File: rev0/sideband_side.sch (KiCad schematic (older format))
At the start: 10 parts

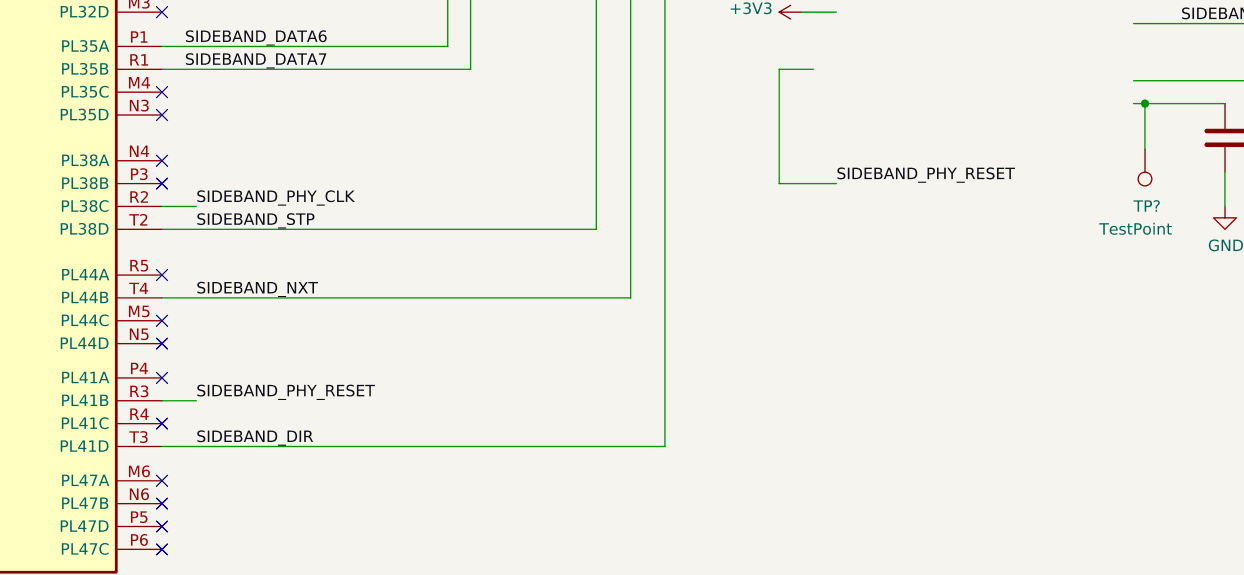
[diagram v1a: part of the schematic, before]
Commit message: schematic: finish initial capture
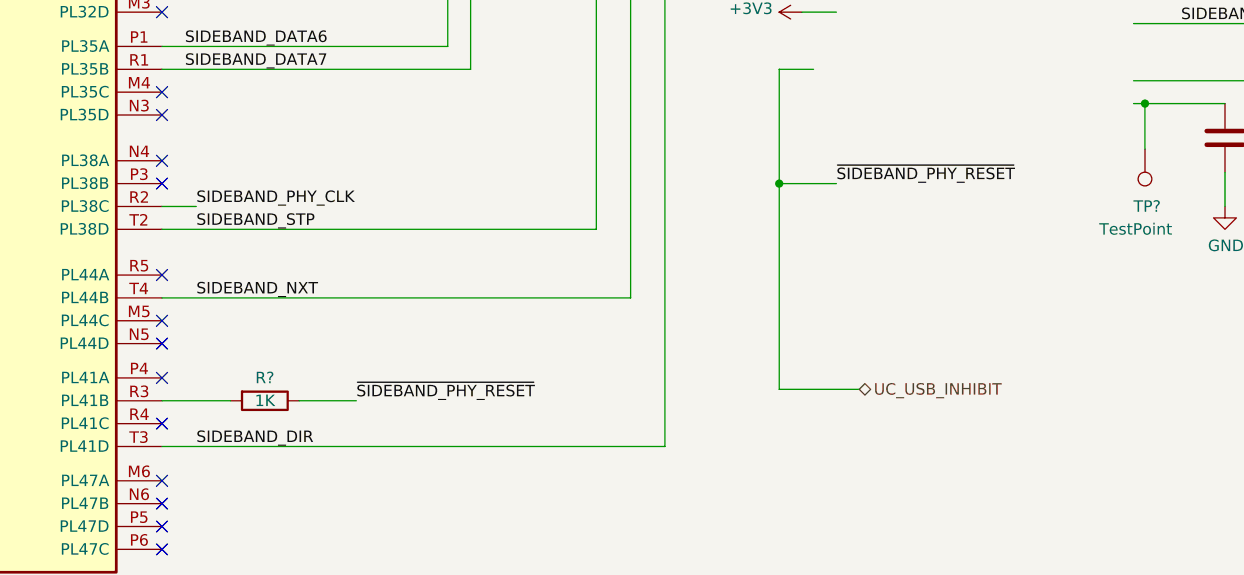
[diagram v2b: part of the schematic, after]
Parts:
- added R?: 1K, symbol Device:R
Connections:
- net labels added: UC_USB_INHIBIT, ~SIDEBAND_PHY_RESET
- net labels removed: SIDEBAND_PHY_RESET
- wire segments 64 -> 67
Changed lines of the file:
@@
 $Descr A4 11693 8268
 encoding utf-8
-Sheet 4 6
-Title "LUNA USB Multitool"
-Date "2019-10-16"
+Sheet 4 9
+Title "LUNA: Sideband USB PHY"
+Date "2019-10-20"
 Rev "r0"
 Comp "Great Scott Gadgets"
 Comment1 "Katherine J. Temkin"
 Comment2 ""
-Comment3 ""
+Comment3 "Licensed under the CERN OHL v1.2"
 Comment4 ""
 $EndDescr
@@
 Text Label 2600 3900 0    50   ~ 0
 SIDEBAND_DATA7
-Text Label 2650 5350 0    50   ~ 0
-SIDEBAND_PHY_RESET
-Wire Wire Line
-	2650 5350 2500 5350
+Text Label 3350 5350 0    50   ~ 0
+~SIDEBAND_PHY_RESET
 Wire Wire Line
 	5450 4400 5200 4400
@@
 	5200 3900 5350 3900
 Text Label 5450 4400 0    50   ~ 0
-SIDEBAND_PHY_RESET
+~SIDEBAND_PHY_RESET
 Text HLabel 8050 3950 2    50   Output ~ 0
 SIDEBAND_PHY_1V8
@@
 NoConn ~ 2500 5900
 NoConn ~ 2500 6000
+Wire Wire Line
+	5200 4400 5200 5300
+Wire Wire Line
+	5200 5300 5550 5300
+Connection ~ 5200 4400
+$Comp
+L Device:R R?
+U 1 1 5E110842
+P 2950 5350
+F 0 "R?" V 2850 5350 50  0000 C CNN
+F 1 "1K" V 2950 5350 50  0000 C CNN
+F 2 "" V 2880 5350 50  0001 C CNN
+F 3 "~" H 2950 5350 50  0001 C CNN
+	1    2950 5350
+	0    1    1    0
+$EndComp
+Wire Wire Line
+	2500 5350 2800 5350
+Wire Wire Line
+	3100 5350 3350 5350
+Text HLabel 5550 5300 2    50   BiDi ~ 0
+UC_USB_INHIBIT
 $EndSCHEMATC

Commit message: rev0: finish capture and start routing (woo!)
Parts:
- added R22: 15K, Resistor_SMD:R_0402_1005Metric, symbol Device:R
- C36, C37: renamed from C?; footprint (none) -> Capacitor_SMD:C_0603_1608Metric
- C38, C39: renamed from C?; footprint (none) -> Capacitor_SMD:C_0402_1005Metric
- IC1: renamed from IC?; footprint BGA256C80P16X16_1400X1400X170 -> luna:lattice_cabga256
- R15, R16, R17: renamed from R?; footprint (none) -> Resistor_SMD:R_0402_1005Metric
- TP5, TP6: renamed from TP?; footprint (none) -> TestPoint:TestPoint_Pad_1.0x1.0mm
- U8: renamed from U?; footprint (none) -> Package_DFN_QFN:VQFN-24-1EP_4x4mm_P0.5mm_EP2.45x2.45mm
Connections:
- net labels added: +3.3V
- wire segments 67 -> 71
- no-connect marks 19 -> 20
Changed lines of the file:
@@
 $EndDescr
 $Comp
-L rhododendron:USB3343 U?
+L rhododendron:USB3343 U8
 U 1 1 5DCDAEF5
 P 5450 2350
-F 0 "U?" H 6050 2513 50  0000 C CNN
+F 0 "U8" H 6050 2513 50  0000 C CNN
 F 1 "USB3343" H 6050 2423 50  0000 C CNN
-F 2 "" H 5450 2350 50  0001 C CNN
+F 2 "Package_DFN_QFN:VQFN-24-1EP_4x4mm_P0.5mm_EP2.45x2.45mm" H 5450 2350 50  0001 C CNN
 F 3 "http://ww1.microchip.com/downloads/en/DeviceDoc/334x.pdf" H 5450 2350 50  0001 C CNN
 	1    5450 2350
@@
 $EndComp
 $Comp
-L fpgas_and_processors:ECP5-BGA256 IC?
+L fpgas_and_processors:ECP5-BGA256 IC1
 U 6 1 5DCE10A7
 P 1550 1900
-F 0 "IC?" H 1520 -167 50  0000 R CNN
+F 0 "IC1" H 1520 -167 50  0000 R CNN
 F 1 "ECP5-BGA256" H 1520 -257 50  0000 R CNN
-F 2 "BGA256C80P16X16_1400X1400X170" H -1650 5350 50  0001 L CNN
+F 2 "luna:lattice_cabga256" H -1650 5350 50  0001 L CNN
 F 3 "" H -2100 6300 50  0001 L CNN
 F 4 "FPGA - Field Programmable Gate Array ECP5; 12k LUTs; 1.1V" H -2100 6200 50  0001 L CNN "Description"
@@
 	1800 1550 1800 1700
 $Comp
-L power:+3V3 #PWR?
+L power:+3V3 #PWR057
 U 1 1 5DD028F3
 P 1750 1450
-F 0 "#PWR?" H 1750 1300 50  0001 C CNN
+F 0 "#PWR057" H 1750 1300 50  0001 C CNN
 F 1 "+3V3" H 1764 1623 50  0000 C CNN
 F 2 "" H 1750 1450 50  0001 C CNN
@@
 Text Label 2650 5550 0    50   ~ 0
 SIDEBAND_DIR
-Wire Wire Line
-	5450 3650 5300 3650
-$Comp
-L power:+3V3 #PWR?
+$Comp
+L power:+3V3 #PWR058
 U 1 1 5DD09124
 P 5300 3650
-F 0 "#PWR?" H 5300 3500 50  0001 C CNN
+F 0 "#PWR058" H 5300 3500 50  0001 C CNN
 F 1 "+3V3" V 5315 3778 50  0000 L CNN
 F 2 "" H 5300 3650 50  0001 C CNN
@@
 SIDEBAND_PHY_1V8
 $Comp
-L Device:C C?
+L Device:C C36
 U 1 1 5DD2517F
 P 7150 4200
-F 0 "C?" H 7265 4245 50  0000 L CNN
+F 0 "C36" H 7265 4245 50  0000 L CNN
 F 1 "1uF" H 7265 4155 50  0000 L CNN
-F 2 "" H 7188 4050 50  0001 C CNN
+F 2 "Capacitor_SMD:C_0603_1608Metric" H 7188 4050 50  0001 C CNN
 F 3 "~" H 7150 4200 50  0001 C CNN
 	1    7150 4200
@@
 $EndComp
 $Comp
-L power:GND #PWR?
+L power:GND #PWR062
 U 1 1 5DD25634
 P 7150 4500
-F 0 "#PWR?" H 7150 4250 50  0001 C CNN
+F 0 "#PWR062" H 7150 4250 50  0001 C CNN
 F 1 "GND" H 7154 4328 50  0000 C CNN
 F 2 "" H 7150 4500 50  0001 C CNN
@@
 	6750 4050 6800 4050
 $Comp
-L Device:C C?
+L Device:C C37
 U 1 1 5DD280CB
 P 7600 4200
-F 0 "C?" H 7715 4245 50  0000 L CNN
+F 0 "C37" H 7715 4245 50  0000 L CNN
 F 1 "1uF" H 7715 4155 50  0000 L CNN
-F 2 "" H 7638 4050 50  0001 C CNN
+F 2 "Capacitor_SMD:C_0603_1608Metric" H 7638 4050 50  0001 C CNN
 F 3 "~" H 7600 4200 50  0001 C CNN
 	1    7600 4200
@@
 $EndComp
 $Comp
-L power:GND #PWR?
+L power:GND #PWR064
 U 1 1 5DD280D5
 P 7600 4500
-F 0 "#PWR?" H 7600 4250 50  0001 C CNN
+F 0 "#PWR064" H 7600 4250 50  0001 C CNN
 F 1 "GND" H 7604 4328 50  0000 C CNN
 F 2 "" H 7600 4500 50  0001 C CNN
@@
 	7600 3950 7850 3950
 $Comp
-L Connector:TestPoint TP?
+L Connector:TestPoint TP6
 U 1 1 5DD2BF2B
 P 7900 3800
-F 0 "TP?" V 7855 3987 50  0000 L CNN
+F 0 "TP6" V 7855 3987 50  0000 L CNN
 F 1 "TestPoint" V 7945 3987 50  0000 L CNN
-F 2 "" H 8100 3800 50  0001 C CNN
+F 2 "TestPoint:TestPoint_Pad_1.0x1.0mm" H 8100 3800 50  0001 C CNN
 F 3 "~" H 8100 3800 50  0001 C CNN
 	1    7900 3800
@@
 	7850 3950 8050 3950
 $Comp
-L Connector:TestPoint TP?
+L Connector:TestPoint TP5
 U 1 1 5DD2DA1C
 P 6800 4250
-F 0 "TP?" H 6850 4500 50  0000 R CNN
+F 0 "TP5" H 6850 4500 50  0000 R CNN
 F 1 "TestPoint" H 7000 4600 50  0000 R CNN
-F 2 "" H 7000 4250 50  0001 C CNN
+F 2 "TestPoint:TestPoint_Pad_1.0x1.0mm" H 7000 4250 50  0001 C CNN
 F 3 "~" H 7000 4250 50  0001 C CNN
 	1    6800 4250
@@
 	6750 2650 6900 2650
 $Comp
-L power:GND #PWR?
+L power:GND #PWR059
 U 1 1 5DD345C7
 P 6900 2650
-F 0 "#PWR?" H 6900 2400 50  0001 C CNN
+F 0 "#PWR059" H 6900 2400 50  0001 C CNN
 F 1 "GND" V 6905 2522 50  0000 R CNN
 F 2 "" H 6900 2650 50  0001 C CNN
@@
 	6950 2450 6950 2200
 $Comp
-L power:+5V #PWR?
+L power:+5V #PWR060
 U 1 1 5DD35DC7
 P 6950 2200
-F 0 "#PWR?" H 6950 2050 50  0001 C CNN
+F 0 "#PWR060" H 6950 2050 50  0001 C CNN
 F 1 "+5V" H 6964 2373 50  0000 C CNN
 F 2 "" H 6950 2200 50  0001 C CNN
@@
 $EndComp
 $Comp
-L power:+3V3 #PWR?
+L power:+3V3 #PWR061
 U 1 1 5DD36515
 P 7150 2200
-F 0 "#PWR?" H 7150 2050 50  0001 C CNN
+F 0 "#PWR061" H 7150 2050 50  0001 C CNN
 F 1 "+3V3" H 7164 2373 50  0000 C CNN
 F 2 "" H 7150 2200 50  0001 C CNN
@@
 	7150 2550 6750 2550
 $Comp
-L Device:R R?
+L Device:R R16
 U 1 1 5DD37F86
 P 7050 3400
-F 0 "R?" V 7000 3250 50  0000 C CNN
+F 0 "R16" V 7000 3200 50  0000 C CNN
 F 1 "8.06k+1%" V 6950 3550 50  0000 C CNN
-F 2 "" V 6980 3400 50  0001 C CNN
+F 2 "Resistor_SMD:R_0402_1005Metric" V 6980 3400 50  0001 C CNN
 F 3 "~" H 7050 3400 50  0001 C CNN
 	1    7050 3400
@@
 	6900 3400 6750 3400
 $Comp
-L power:GND #PWR?
+L power:GND #PWR063
 U 1 1 5DD39A7C
 P 7400 3400
-F 0 "#PWR?" H 7400 3150 50  0001 C CNN
+F 0 "#PWR063" H 7400 3150 50  0001 C CNN
 F 1 "GND" V 7405 3272 50  0000 R CNN
 F 2 "" H 7400 3400 50  0001 C CNN
@@
 	7400 3400 7200 3400
 $Comp
-L Device:R R?
+L Device:R R17
 U 1 1 5DD3B600
 P 7100 2850
-F 0 "R?" V 7050 2700 50  0000 C CNN
+F 0 "R17" V 7050 2650 50  0000 C CNN
 F 1 "20k" V 7100 2850 50  0000 C CNN
-F 2 "" V 7030 2850 50  0001 C CNN
+F 2 "Resistor_SMD:R_0402_1005Metric" V 7030 2850 50  0001 C CNN
 F 3 "~" H 7100 2850 50  0001 C CNN
 	1    7100 2850
@@
 	7250 2850 7450 2850
 $Comp
-L Device:C C?
+L Device:C C38
 U 1 1 5DD3F3AE
 P 8600 1550
-F 0 "C?" H 8715 1595 50  0000 L CNN
+F 0 "C38" H 8715 1595 50  0000 L CNN
 F 1 "0.1uF" H 8715 1505 50  0000 L CNN
-F 2 "" H 8638 1400 50  0001 C CNN
+F 2 "Capacitor_SMD:C_0402_1005Metric" H 8638 1400 50  0001 C CNN
 F 3 "~" H 8600 1550 50  0001 C CNN
 	1    8600 1550
@@
 $EndComp
 $Comp
-L Device:C C?
+L Device:C C39
 U 1 1 5DD3FB40
 P 9100 1550
-F 0 "C?" H 9215 1595 50  0000 L CNN
+F 0 "C39" H 9215 1595 50  0000 L CNN
 F 1 "0.1uF" H 9215 1505 50  0000 L CNN
-F 2 "" H 9138 1400 50  0001 C CNN
+F 2 "Capacitor_SMD:C_0402_1005Metric" H 9138 1400 50  0001 C CNN
 F 3 "~" H 9100 1550 50  0001 C CNN
 	1    9100 1550
@@
 $EndComp
 $Comp
-L power:+5V #PWR?
+L power:+5V #PWR065
 U 1 1 5DD40529
 P 8600 1300
-F 0 "#PWR?" H 8600 1150 50  0001 C CNN
+F 0 "#PWR065" H 8600 1150 50  0001 C CNN
 F 1 "+5V" H 8614 1473 50  0000 C CNN
 F 2 "" H 8600 1300 50  0001 C CNN
@@
 $EndComp
 $Comp
-L power:+3V3 #PWR?
+L power:+3V3 #PWR067
 U 1 1 5DD40800
 P 9100 1300
-F 0 "#PWR?" H 9100 1150 50  0001 C CNN
+F 0 "#PWR067" H 9100 1150 50  0001 C CNN
 F 1 "+3V3" H 9114 1473 50  0000 C CNN
 F 2 "" H 9100 1300 50  0001 C CNN
@@
 $EndComp
 $Comp
-L power:GND #PWR?
+L power:GND #PWR066
 U 1 1 5DD40C56
 P 8600 1800
-F 0 "#PWR?" H 8600 1550 50  0001 C CNN
+F 0 "#PWR066" H 8600 1550 50  0001 C CNN
 F 1 "GND" H 8604 1628 50  0000 C CNN
 F 2 "" H 8600 1800 50  0001 C CNN
@@
 $EndComp
 $Comp
-L power:GND #PWR?
+L power:GND #PWR068
 U 1 1 5DD410FE
 P 9100 1800
-F 0 "#PWR?" H 9100 1550 50  0001 C CNN
+F 0 "#PWR068" H 9100 1550 50  0001 C CNN
 F 1 "GND" H 9104 1628 50  0000 C CNN
 F 2 "" H 9100 1800 50  0001 C CNN
@@
 NoConn ~ 2500 6000
 Wire Wire Line
-	5200 4400 5200 5300
+	5200 4400 5200 4850
 Wire Wire Line
 	5200 5300 5550 5300
 Connection ~ 5200 4400
 $Comp
-L Device:R R?
+L Device:R R15
 U 1 1 5E110842
 P 2950 5350
-F 0 "R?" V 2850 5350 50  0000 C CNN
+F 0 "R15" V 2850 5350 50  0000 C CNN
 F 1 "1K" V 2950 5350 50  0000 C CNN
-F 2 "" V 2880 5350 50  0001 C CNN
+F 2 "Resistor_SMD:R_0402_1005Metric" V 2880 5350 50  0001 C CNN
 F 3 "~" H 2950 5350 50  0001 C CNN
 	1    2950 5350
@@
 Wire Wire Line
 	3100 5350 3350 5350
-Text HLabel 5550 5300 2    50   BiDi ~ 0
+Wire Wire Line
+	5450 3650 5300 3650
+Text HLabel 5550 5300 2    50   Input ~ 0
 UC_USB_INHIBIT
+$Comp
+L Device:R R?
+U 1 1 5E1591E2
+P 4900 4600
+AR Path="/5DD754D4/5E1591E2" Ref="R?"  Part="1"
+AR Path="/5DCD9772/5E1591E2" Ref="R22"  Part="1"
+F 0 "R22" V 5000 4600 50  0000 C CNN
+F 1 "15K" V 4900 4600 50  0000 C CNN
+F 2 "Resistor_SMD:R_0402_1005Metric" V 4830 4600 50  0001 C CNN
+F 3 "~" H 4900 4600 50  0001 C CNN
+	1    4900 4600
+	-1   0    0    1
+$EndComp
+Wire Wire Line
+	4900 4750 4900 4850
+Wire Wire Line
+	4900 4450 4900 4350
+$Comp
+L ibp-hyperram-cache:+3.3V #PWR?
+U 1 1 5E1591EA
+P 4900 4350
+AR Path="/5DD754D4/5E1591EA" Ref="#PWR?"  Part="1"
+AR Path="/5DCD9772/5E1591EA" Ref="#PWR099"  Part="1"
+F 0 "#PWR099" H 4900 4200 50  0001 C CNN
+F 1 "+3.3V" V 4915 4478 50  0000 L CNN
+F 2 "" H 4900 4350 50  0001 C CNN
+F 3 "" H 4900 4350 50  0001 C CNN
+	1    4900 4350
+	1    0    0    -1
+$EndComp
+Wire Wire Line
+	4900 4850 5200 4850
+Connection ~ 5200 4850
+Wire Wire Line
+	5200 4850 5200 5300
+NoConn ~ 6750 3600
 $EndSCHEMATC

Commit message: rev0: clean up library references and backup files
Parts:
- U8: symbol rhododendron:USB3343 -> usb:USB3343
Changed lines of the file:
@@
 EESchema Schematic File Version 4
 LIBS:luna_rev0-cache
-EELAYER 29 0
+EELAYER 30 0
 EELAYER END
 $Descr A4 11693 8268
@@
 $EndDescr
 $Comp
-L rhododendron:USB3343 U8
+L usb:USB3343 U8
 U 1 1 5DCDAEF5
 P 5450 2350
@@
 	4900 4450 4900 4350
 $Comp
-L ibp-hyperram-cache:+3.3V #PWR?
+L support_hardware:S27KS0641 #PWR?
 U 1 1 5E1591EA
 P 4900 4350
 AR Path="/5DD754D4/5E1591EA" Ref="#PWR?"  Part="1"
 AR Path="/5DCD9772/5E1591EA" Ref="#PWR099"  Part="1"
+AR Path="/5E1591EA" Ref="#PWR099"  Part="1"
 F 0 "#PWR099" H 4900 4200 50  0001 C CNN
 F 1 "+3.3V" V 4915 4478 50  0000 L CNN

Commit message: rev0: throw the parts down so we can get starting routing
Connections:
- net +3V3: now also R22.2
- net SIDEBAND_DATA0: now also IC1.R2 (PL38C); no longer IC1.L1 (PL26A)
- net SIDEBAND_DATA1: now also IC1.R1 (PL35B); no longer IC1.L2 (PL26B)
- net SIDEBAND_DATA2: now also IC1.P2 (PL32B); no longer IC1.M1 (PL26C)
- net SIDEBAND_DATA3: now also IC1.P1 (PL35A); no longer IC1.M2 (PL26D)
- net SIDEBAND_DATA5: now also IC1.M2 (PL26D); no longer IC1.P2 (PL32B)
- net SIDEBAND_DATA6: now also IC1.M1 (PL26C); no longer IC1.P1 (PL35A)
- net SIDEBAND_DATA7: now also IC1.L2 (PL26B); no longer IC1.R1 (PL35B)
- net SIDEBAND_NXT: now also IC1.T2 (PL38D); no longer IC1.T4 (PL44B)
- net SIDEBAND_PHY_CLK: now also IC1.L1 (PL26A); no longer IC1.R2 (PL38C)
- net SIDEBAND_STP: now also IC1.T4 (PL44B); no longer IC1.T2 (PL38D)
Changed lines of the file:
@@
 Wire Wire Line
 	1750 1550 1800 1550
-Wire Wire Line
-	5450 3550 4700 3550
-Wire Wire Line
-	4700 3550 4700 5550
-Wire Wire Line
-	5450 3450 4550 3450
-Wire Wire Line
-	4550 3450 4550 4900
-Wire Wire Line
-	5450 3350 4400 3350
-Wire Wire Line
-	4400 3350 4400 4600
 Text Label 2650 4600 0    50   ~ 0
+SIDEBAND_NXT
+Text Label 2650 4900 0    50   ~ 0
 SIDEBAND_STP
-Text Label 2650 4900 0    50   ~ 0
-SIDEBAND_NXT
 Text Label 2650 5550 0    50   ~ 0
 SIDEBAND_DIR
@@
 	0    -1   -1   0
 $EndComp
-Wire Wire Line
-	2500 4600 4400 4600
-Wire Wire Line
-	2500 4900 4550 4900
-Wire Wire Line
-	2500 5550 4700 5550
-Wire Wire Line
-	5450 3150 3850 3150
-Wire Wire Line
-	3850 3150 3850 3900
-Wire Wire Line
-	3850 3900 2500 3900
-Wire Wire Line
-	5450 3050 3750 3050
-Wire Wire Line
-	3750 3050 3750 3800
-Wire Wire Line
-	3750 3800 2500 3800
-Wire Wire Line
-	5450 2950 3650 2950
-Wire Wire Line
-	3650 2950 3650 3450
-Wire Wire Line
-	3650 3450 2500 3450
-Wire Wire Line
-	3550 2850 3550 3350
-Wire Wire Line
-	3550 3350 2500 3350
-Wire Wire Line
-	3550 2850 5450 2850
-Wire Wire Line
-	2500 2750 5450 2750
-Wire Wire Line
-	5450 2650 2500 2650
-Wire Wire Line
-	5450 2550 2500 2550
-Wire Wire Line
-	5450 2450 2500 2450
-Text Label 2600 2450 0    50   ~ 0
+Text Label 4500 2450 0    50   ~ 0
 SIDEBAND_DATA0
-Text Label 2600 2550 0    50   ~ 0
+Text Label 4500 2550 0    50   ~ 0
 SIDEBAND_DATA1
-Text Label 2600 2650 0    50   ~ 0
+Text Label 4500 2650 0    50   ~ 0
 SIDEBAND_DATA2
-Text Label 2600 2750 0    50   ~ 0
+Text Label 4500 2750 0    50   ~ 0
 SIDEBAND_DATA3
 NoConn ~ 2500 2900
@@
 Text Label 7650 3700 2    50   ~ 0
 SIDEBAND_PHY_CLK
-Text Label 2650 4500 0    50   ~ 0
+Text Label 2650 2450 0    50   ~ 0
 SIDEBAND_PHY_CLK
-Wire Wire Line
-	2500 4500 2650 4500
-Text Label 2600 3350 0    50   ~ 0
+Text Label 4500 2850 0    50   ~ 0
 SIDEBAND_DATA4
-Text Label 2600 3450 0    50   ~ 0
+Text Label 4500 2950 0    50   ~ 0
 SIDEBAND_DATA5
-Text Label 2600 3800 0    50   ~ 0
+Text Label 4500 3050 0    50   ~ 0
 SIDEBAND_DATA6
-Text Label 2600 3900 0    50   ~ 0
+Text Label 4500 3150 0    50   ~ 0
 SIDEBAND_DATA7
 Text Label 3350 5350 0    50   ~ 0
@@
 Wire Wire Line
 	4900 4450 4900 4350
-$Comp
-L support_hardware:S27KS0641 #PWR?
-U 1 1 5E1591EA
+Wire Wire Line
+	4900 4850 5200 4850
+Connection ~ 5200 4850
+Wire Wire Line
+	5200 4850 5200 5300
+NoConn ~ 6750 3600
+$Comp
+L power:+3V3 #PWR0108
+U 1 1 5DE2FBF8
 P 4900 4350
-AR Path="/5DD754D4/5E1591EA" Ref="#PWR?"  Part="1"
-AR Path="/5DCD9772/5E1591EA" Ref="#PWR099"  Part="1"
-AR Path="/5E1591EA" Ref="#PWR099"  Part="1"
-F 0 "#PWR099" H 4900 4200 50  0001 C CNN
-F 1 "+3.3V" V 4915 4478 50  0000 L CNN
+F 0 "#PWR0108" H 4900 4200 50  0001 C CNN
+F 1 "+3V3" H 4915 4523 50  0000 C CNN
 F 2 "" H 4900 4350 50  0001 C CNN
 F 3 "" H 4900 4350 50  0001 C CNN
@@
 $EndComp
 Wire Wire Line
-	4900 4850 5200 4850
-Connection ~ 5200 4850
-Wire Wire Line
-	5200 4850 5200 5300
-NoConn ~ 6750 3600
+	2500 4600 4100 4600
+Wire Wire Line
+	2500 4900 4100 4900
+Wire Wire Line
+	2500 5550 4100 5550
+Entry Wire Line
+	4100 5550 4200 5450
+Entry Wire Line
+	4100 4900 4200 4800
+Entry Wire Line
+	4100 4600 4200 4500
+Entry Wire Line
+	4200 3450 4300 3350
+Wire Wire Line
+	4300 3350 5450 3350
+Wire Wire Line
+	4300 3450 5450 3450
+Entry Wire Line
+	4300 3450 4200 3550
+Wire Wire Line
+	4300 3550 5450 3550
+Entry Wire Line
+	4300 3550 4200 3650
+Text Label 4500 3350 0    50   ~ 0
+SIDEBAND_STP
+Text Label 4500 3450 0    50   ~ 0
+SIDEBAND_NXT
+Text Label 4500 3550 0    50   ~ 0
+SIDEBAND_DIR
+Wire Wire Line
+	5450 2450 4300 2450
+Entry Wire Line
+	4300 2450 4200 2550
+Wire Wire Line
+	5450 2550 4300 2550
+Wire Wire Line
+	5450 2650 4300 2650
+Wire Wire Line
+	5450 2750 4300 2750
+Wire Wire Line
+	5450 2850 4300 2850
+Wire Wire Line
+	5450 2950 4300 2950
+Wire Wire Line
+	5450 3050 4300 3050
+Wire Wire Line
+	5450 3150 4300 3150
+Entry Wire Line
+	4200 2650 4300 2550
+Entry Wire Line
+	4200 2750 4300 2650
+Entry Wire Line
+	4200 2850 4300 2750
+Entry Wire Line
+	4200 2950 4300 2850
+Entry Wire Line
+	4200 3050 4300 2950
+Entry Wire Line
+	4200 3150 4300 3050
+Entry Wire Line
+	4200 3250 4300 3150
+Wire Wire Line
+	2500 3800 4100 3800
+Entry Wire Line
+	4100 3800 4200 3700
+Wire Wire Line
+	2500 3900 4100 3900
+Entry Wire Line
+	4100 3900 4200 3800
+Wire Wire Line
+	2500 3450 4100 3450
+Wire Wire Line
+	2500 3350 4100 3350
+Entry Wire Line
+	4100 3350 4200 3250
+Entry Wire Line
+	4100 3450 4200 3350
+Wire Wire Line
+	2500 2750 4100 2750
+Wire Wire Line
+	2500 2650 4100 2650
+Wire Wire Line
+	2500 2550 4100 2550
+Entry Wire Line
+	4100 2550 4200 2450
+Entry Wire Line
+	4100 2650 4200 2550
+Entry Wire Line
+	4100 2750 4200 2650
+Entry Wire Line
+	4100 4500 4200 4400
+Wire Wire Line
+	2500 4500 4100 4500
+Text Label 2650 4500 0    50   ~ 0
+SIDEBAND_DATA0
+Text Label 2650 3900 0    50   ~ 0
+SIDEBAND_DATA1
+Text Label 2650 3450 0    50   ~ 0
+SIDEBAND_DATA2
+Text Label 2650 3800 0    50   ~ 0
+SIDEBAND_DATA3
+Text Label 2650 3350 0    50   ~ 0
+SIDEBAND_DATA4
+Text Label 2650 2750 0    50   ~ 0
+SIDEBAND_DATA5
+Text Label 2650 2650 0    50   ~ 0
+SIDEBAND_DATA6
+Text Label 2650 2550 0    50   ~ 0
+SIDEBAND_DATA7
+Wire Wire Line
+	2500 2450 2650 2450
+Wire Bus Line
+	4200 2350 4200 5450
 $EndSCHEMATC
